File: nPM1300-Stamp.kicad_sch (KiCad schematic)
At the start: 16 parts, among them J1 Conn_01x08, J2 Conn_01x08, J3 Conn_01x08, J4 Conn_01x08, U1 nPM1300-QEXX

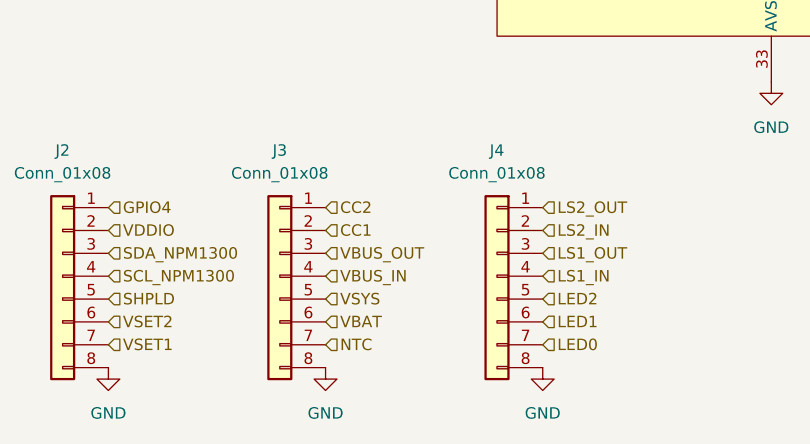
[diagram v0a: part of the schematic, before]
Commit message: Added nPM1300 library
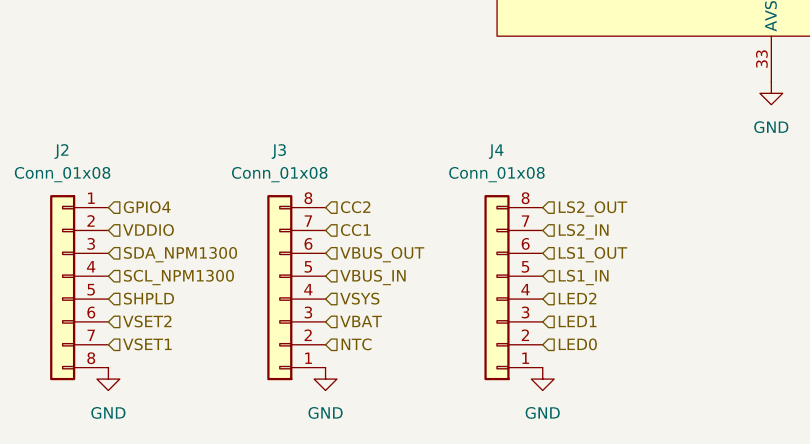
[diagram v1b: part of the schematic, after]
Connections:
- net CC1: now also J3.7 (Pin_7); no longer J3.2 (Pin_2)
- net CC2: now also J3.8 (Pin_8); no longer J3.1 (Pin_1)
- net GND: now also J3.1 (Pin_1), J4.1 (Pin_1); no longer J3.8 (Pin_8), J4.8 (Pin_8)
- net LED0: now also J4.2 (Pin_2); no longer J4.7 (Pin_7)
- net LED1: now also J4.3 (Pin_3); no longer J4.6 (Pin_6)
- net LED2: now also J4.4 (Pin_4); no longer J4.5 (Pin_5)
- net LS1_IN: now also J4.5 (Pin_5); no longer J4.4 (Pin_4)
- net LS1_OUT: now also J4.6 (Pin_6); no longer J4.3 (Pin_3)
- net LS2_IN: now also J4.7 (Pin_7); no longer J4.2 (Pin_2)
- net LS2_OUT: now also J4.8 (Pin_8); no longer J4.1 (Pin_1)
- net NTC: now also J3.2 (Pin_2); no longer J3.7 (Pin_7)
- net VBAT: now also J3.3 (Pin_3); no longer J3.6 (Pin_6)
- net VBUS_IN: now also J3.5 (Pin_5); no longer J3.4 (Pin_4)
- net VBUS_OUT: now also J3.6 (Pin_6); no longer J3.3 (Pin_3)
- net VSYS: now also J3.4 (Pin_4); no longer J3.5 (Pin_5)
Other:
- moved on the sheet: J3, J4
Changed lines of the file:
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@@
 	(symbol
 		(lib_id "Connector_Generic:Conn_01x08")
-		(at 111.76 153.67 0)
-		(mirror y)
-		(unit 1)
-		(exclude_from_sim no)
-		(in_bom yes)
-		(on_board yes)
-		(dnp no)
-		(fields_autoplaced yes)
+		(at 111.76 156.21 180)
+		(unit 1)
+		(exclude_from_sim no)
+		(in_bom yes)
+		(on_board yes)
+		(dnp no)
 		(property "Reference" "J4"
 			(at 111.76 139.7 0)
@@
 		)
 		(property "Footprint" "nPM1300-Stamp_Connector_PinHeader:nPM1300-PinHeader_1x08_P2.00mm_Vertical"
-			(at 111.76 153.67 0)
+			(at 111.76 156.21 0)
 			(effects
 				(font
@@
 		)
 		(property "Datasheet" "~"
-			(at 111.76 153.67 0)
+			(at 111.76 156.21 0)
 			(effects
 				(font
@@
 		)
 		(property "Description" "Generic connector, single row, 01x08, script generated (kicad-library-utils/schlib/autogen/connector/)"
-			(at 111.76 153.67 0)
+			(at 111.76 156.21 0)
 			(effects
 				(font
@@
 	(symbol
 		(lib_id "Connector_Generic:Conn_01x08")
-		(at 87.63 153.67 0)
-		(mirror y)
-		(unit 1)
-		(exclude_from_sim no)
-		(in_bom yes)
-		(on_board yes)
-		(dnp no)
-		(fields_autoplaced yes)
+		(at 87.63 156.21 180)
+		(unit 1)
+		(exclude_from_sim no)
+		(in_bom yes)
+		(on_board yes)
+		(dnp no)
 		(property "Reference" "J3"
 			(at 87.63 139.7 0)
@@
 		)
 		(property "Footprint" "nPM1300-Stamp_Connector_PinHeader:nPM1300-PinHeader_1x08_P2.00mm_Vertical"
-			(at 87.63 153.67 0)
+			(at 87.63 156.21 0)
 			(effects
 				(font
@@
 		)
 		(property "Datasheet" "~"
-			(at 87.63 153.67 0)
+			(at 87.63 156.21 0)
 			(effects
 				(font
@@
 		)
 		(property "Description" "Generic connector, single row, 01x08, script generated (kicad-library-utils/schlib/autogen/connector/)"
-			(at 87.63 153.67 0)
-			(effects
-				(font
+			(at 87.63 156.21 0)
+			(effects
+				(font

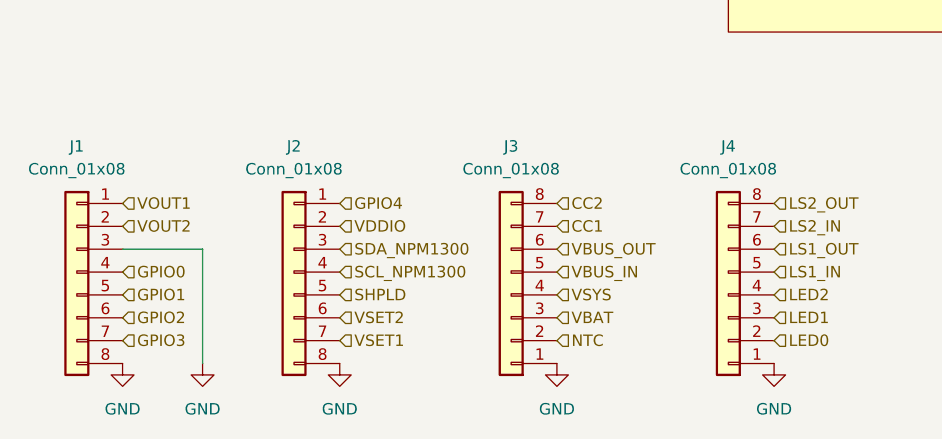
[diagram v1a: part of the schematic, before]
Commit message: Added JLCPCB production files
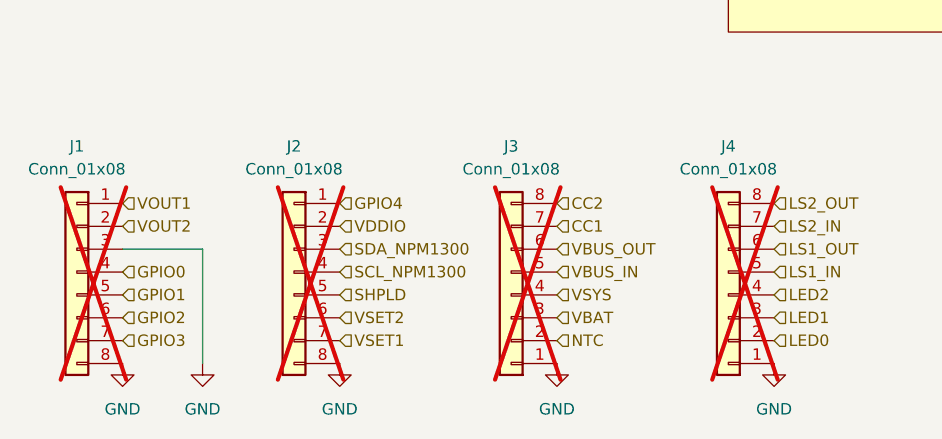
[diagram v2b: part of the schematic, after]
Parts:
- C1: LCSC (none) -> C307331
- C13: LCSC (none) -> C50254
- C2, C3, C4, C7, C8: LCSC (none) -> C19702
- C5, C6: LCSC (none) -> C15849
- J1, J2, J3, J4: now not fitted
- L1, L2: LCSC (none) -> C354533
- U1: LCSC (none) -> C7466043
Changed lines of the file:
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@@
+			)
+		)
+		(property "LCSC" "C19702"
+			(at 196.85 76.2 0)
+			(effects
+				(font
+					(size 1.27 1.27)
+				)
+				(hide yes)
 			)
 		)
@@
 			)
 		)
+		(property "LCSC" "C50254"
+			(at 187.96 124.46 0)
+			(effects
+				(font
+					(size 1.27 1.27)
+				)
+				(hide yes)
+			)
+		)
 		(pin "1"
 		)
@@
 		(in_bom yes)
 		(on_board yes)
-		(dnp no)
+		(dnp yes)
 		(fields_autoplaced yes)
 		(property "Reference" "J2"
@@
 			)
 		)
+		(property "LCSC" ""
+			(at 63.5 153.67 0)
+			(effects
+				(font
+					(size 1.27 1.27)
+				)
+				(hide yes)
+			)
+		)
 		(pin "1"
 		)
@@
 			)
 		)
+		(property "LCSC" "C19702"
+			(at 152.4 41.91 0)
+			(effects
+				(font
+					(size 1.27 1.27)
+				)
+				(hide yes)
+			)
+		)
 		(pin "1"
 		)
@@
 		(in_bom yes)
 		(on_board yes)
-		(dnp no)
+		(dnp yes)
 		(property "Reference" "J4"
 			(at 111.76 139.7 0)
@@
 			)
 		)
+		(property "LCSC" ""
+			(at 111.76 156.21 0)
+			(effects
+				(font
+					(size 1.27 1.27)
+				)
+				(hide yes)
+			)
+		)
 		(pin "1"
 		)
@@
 		)
 		(property "Description" "Unpolarized capacitor, small symbol"
+			(at 134.62 41.91 0)
+			(effects
+				(font
+					(size 1.27 1.27)
+				)
+				(hide yes)
+			)
+		)
+		(property "LCSC" "C307331"
 			(at 134.62 41.91 0)
 			(effects
@@
 			)
 		)
+		(property "LCSC" "C15849"
+			(at 96.52 60.96 0)
+			(effects
+				(font
+					(size 1.27 1.27)
+				)
+				(hide yes)
+			)
+		)
 		(pin "1"
 		)
@@
 			)
 		)
+		(property "LCSC" "C354533"
+			(at 185.42 76.2 0)
+			(effects
+				(font
+					(size 1.27 1.27)
+				)
+				(hide yes)
+			)
+		)
 		(pin "2"
 		)
@@
 		(in_bom yes)
 		(on_board yes)
-		(dnp no)
+		(dnp yes)
 		(property "Reference" "J3"
 			(at 87.63 139.7 0)
@@
 		)
 		(property "Description" "Generic connector, single row, 01x08, script generated (kicad-library-utils/schlib/autogen/connector/)"
+			(at 87.63 156.21 0)
+			(effects
+				(font
+					(size 1.27 1.27)
+				)
+				(hide yes)
+			)
+		)
+		(property "LCSC" ""
 			(at 87.63 156.21 0)
 			(effects
@@
 			)
 		)
+		(property "LCSC" "C19702"
+			(at 162.56 41.91 0)
+			(effects
+				(font
+					(size 1.27 1.27)
+				)
+				(hide yes)
+			)
+		)
 		(pin "1"
 		)
@@
 		(in_bom yes)
 		(on_board yes)
-		(dnp no)
+		(dnp yes)
 		(fields_autoplaced yes)
 		(property "Reference" "J1"
@@
 		)
 		(property "Description" "Generic connector, single row, 01x08, script generated (kicad-library-utils/schlib/autogen/connector/)"
+			(at 39.37 153.67 0)
+			(effects
+				(font
+					(size 1.27 1.27)
+				)
+				(hide yes)
+			)
+		)
+		(property "LCSC" ""
 			(at 39.37 153.67 0)
 			(effects
@@
 			)
 		)
+		(property "LCSC" "C7466043"
+			(at 142.24 91.44 0)
+			(effects
+				(font
+					(size 1.27 1.27)
+				)
+				(hide yes)
+			)
+		)
 		(pin "14"
 		)
@@
 			)
 		)
+		(property "LCSC" "C19702"
+			(at 172.72 41.91 0)
+			(effects
+				(font
+					(size 1.27 1.27)
+				)
+				(hide yes)
+			)
+		)
 		(pin "1"
 		)
@@
 			)
 		)
+		(property "LCSC" "C15849"
+			(at 187.96 62.23 0)
+			(effects
+				(font
+					(size 1.27 1.27)
+				)
+				(hide yes)
+			)
+		)
 		(pin "1"
 		)
@@
 			)
 		)
+		(property "LCSC" "C354533"
+			(at 196.85 88.9 0)
+			(effects
+				(font
+					(size 1.27 1.27)
+				)
+				(hide yes)
+			)
+		)
 		(pin "2"
 		)
@@
 			(at 208.28 88.9 0)
 			(effects
+				(font
+					(size 1.27 1.27)
+				)
+				(hide yes)
+			)
+		)
+		(property "LCSC" "C19702"
+			(at 208.28 88.9 0)
+			(effects

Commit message: Updated LCSC part number for 2.2uF cap
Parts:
- C13: LCSC C50254 -> C23630
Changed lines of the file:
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@@
 			)
 		)
-		(property "LCSC" "C50254"
+		(property "LCSC" "C23630"
 			(at 187.96 124.46 0)
 			(effects
